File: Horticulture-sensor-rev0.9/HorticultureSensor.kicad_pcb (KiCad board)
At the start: 2 copper layers, 23 parts, among them J1 Conn_01x04, J2 Conn_02x05_Odd_Even, J3 Conn_01x03, J4 Conn_01x04, J5 Conn_01x03, J6 Conn_01x02, J7 Conn_01x02, J8 Conn_01x01_MountingPin, J9 Conn_01x01_MountingPin, Q1 IRLML2030TRPBF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

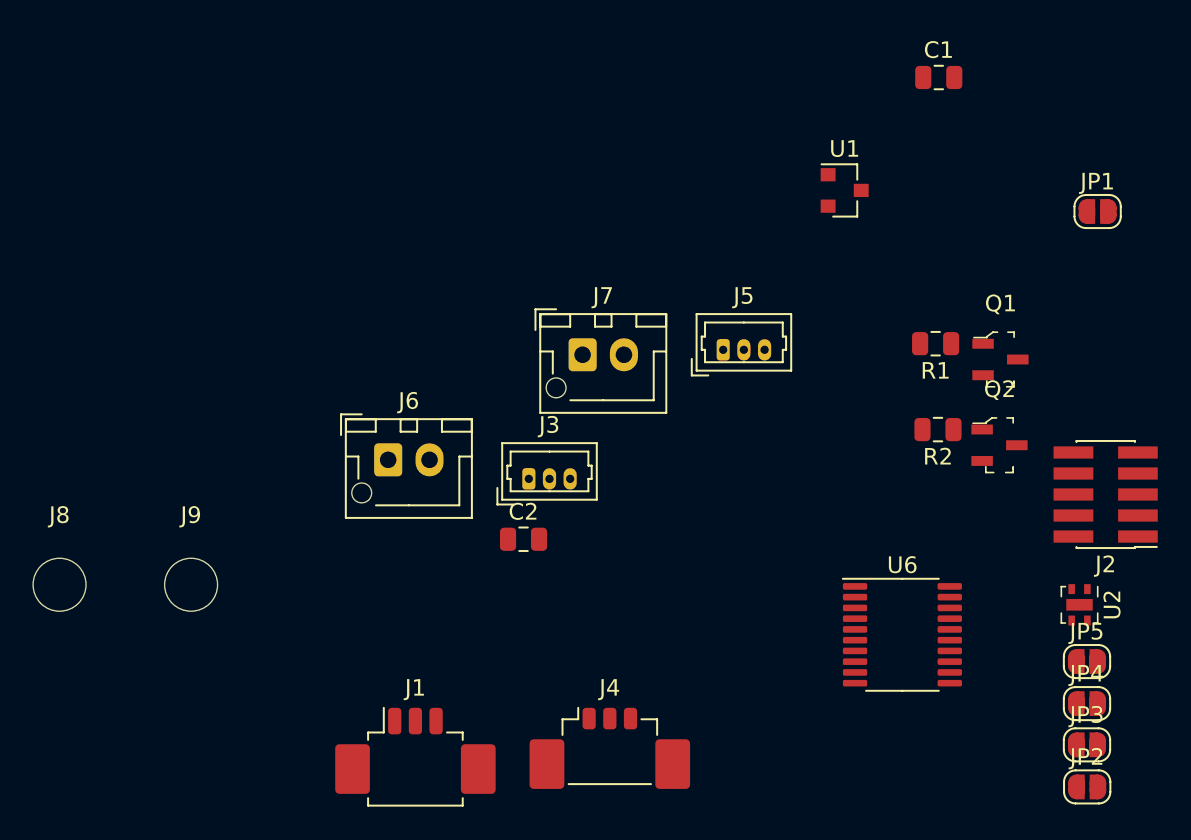
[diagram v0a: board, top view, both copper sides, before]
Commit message: Initial sensor design
Almost finished, need to work out how power connection should work.
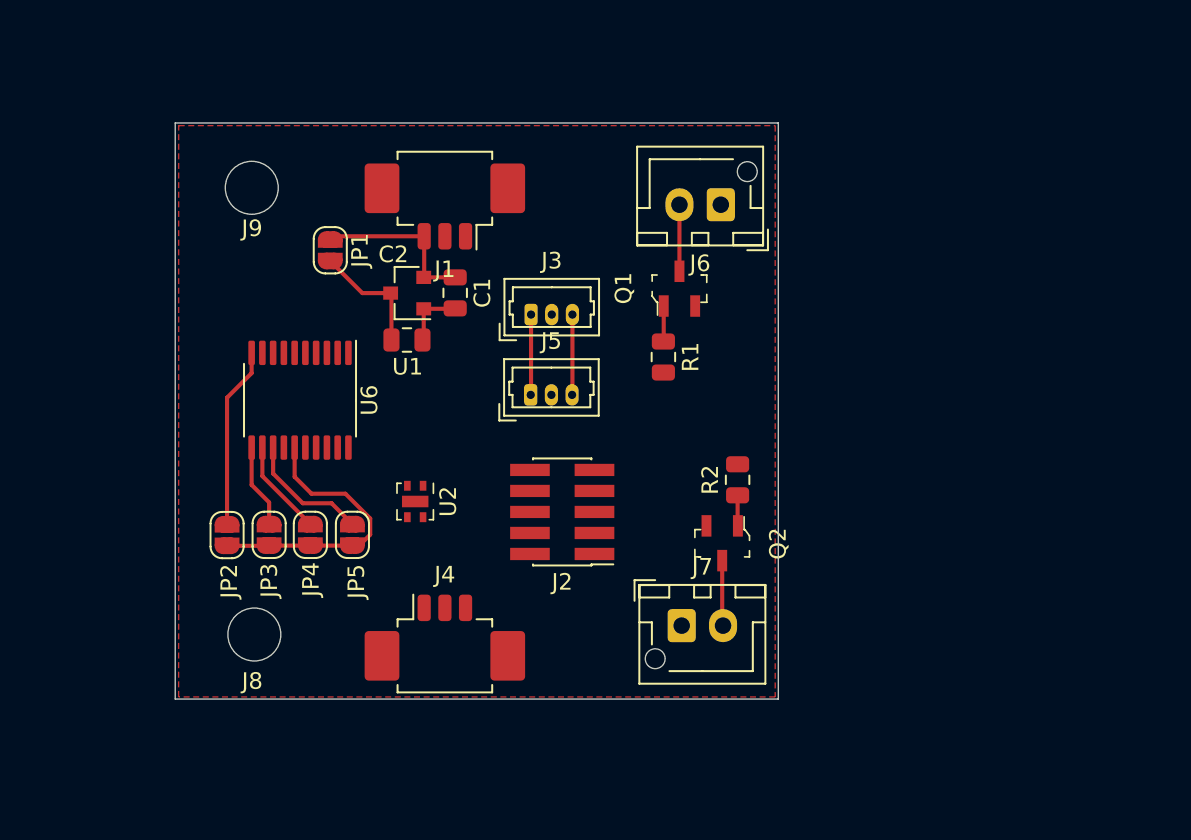
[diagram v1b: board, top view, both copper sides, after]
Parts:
- J4: footprint Connector_Molex:Molex_PicoBlade_53398-0371_1x03-1MP_P1.25mm_Vertical -> Connector_Molex:Molex_PicoBlade_53261-0371_1x03-1MP_P1.25mm_Horizontal
- moved JP2 54.2 mm to (146.7, 136.0), turned to 270 degrees
- moved JP3 51.0 mm to (149.2, 136.0), turned to 270 degrees
- moved JP4 48.0 mm to (151.7, 136.0), turned to 270 degrees
- moved JP1 46.4 mm to (152.9, 118.8), turned to 270 degrees
- moved JP5 45.1 mm to (154.3, 136.0), turned to 270 degrees
- moved U2 40.6 mm to (158.1, 134.0)
- moved U6 39.1 mm to (151.1, 127.8), turned to 270 degrees
- moved J1 34.1 mm to (159.8, 115.5), turned to 180 degrees
- moved J2 32.9 mm to (166.9, 134.6)
- moved C1 32.0 mm to (160.5, 121.4), turned to 270 degrees
- moved U1 27.2 mm to (157.6, 121.4), turned to 180 degrees
- moved J6 25.3 mm to (176.5, 116.0), turned to 180 degrees
- moved J9 24.3 mm to (148.2, 115.0)
- moved Q1 19.9 mm to (174.0, 121.1), turned to 90 degrees
- moved Q2 17.8 mm to (176.6, 136.5), turned to 270 degrees
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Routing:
- net GND: track 0.00 -> 26.0 mm
- net +3V3: track 0.00 -> 12.2 mm
- net i2c-addr_0: track 0.00 -> 11.0 mm
- net VCC: track 0.00 -> 10.2 mm
- net i2c-addr_3: track 0.00 -> 7.63 mm
- net i2c-addr_2: track 0.00 -> 5.83 mm
- net i2c-addr_1: track 0.00 -> 5.06 mm
- net control_0: track 0.00 -> 4.02 mm
- net control_1: track 0.00 -> 3.95 mm
- net Net-(Q1-Pad1): track 0.00 -> 2.15 mm
- net Net-(Q2-Pad1): track 0.00 -> 1.85 mm
- added copper zone on F.Cu, net GND
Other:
- board outline added: 36.5 x 34.8 mm

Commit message: Working on sensor board
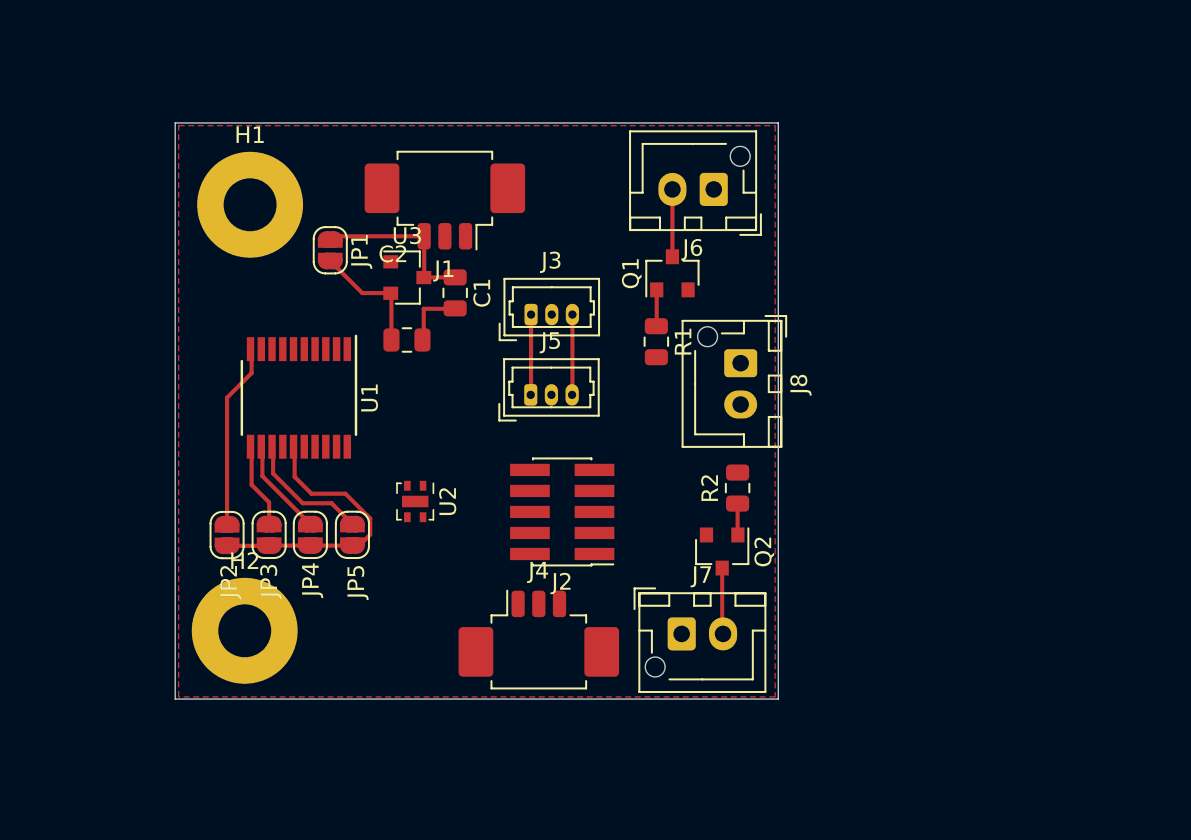
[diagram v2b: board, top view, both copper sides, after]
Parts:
- removed J9: Conn_01x01_MountingPin, MountingHole:MountingHole_3.2mm_M3
- removed U6: STM32F030F4Px, Package_SO:TSSOP-20_4.4x6.5mm_P0.65mm
- added H1: MountingHole_Pad, MountingHole:MountingHole_3.2mm_M3_Pad, F.Cu at (148.1, 116.0)
- added H2: MountingHole_Pad, MountingHole:MountingHole_3.2mm_M3_Pad, F.Cu at (147.8, 141.8)
- added U3: MCP1700-3302E_TO, Package_TO_SOT_SMD:SOT-23, F.Cu at (157.6, 120.4)
- J8: value Conn_01x01_MountingPin -> Conn_01x02; footprint MountingHole:MountingHole_3.2mm_M3 -> Connector_JST:JST_XH_B2B-XH-AM_1x02_P2.50mm_Vertical
- Q1, Q2: footprint digikey-footprints:SOT-23-3 -> Package_TO_SOT_SMD:SOT-23
- U1: value MCP1700-3302E_TO -> STM32F030F4Px; footprint Package_TO_SOT_SMD:SOT-23 -> Package_SO:TSSOP-20_4.4x6.5mm_P0.65mm
- moved J8 33.7 mm to (177.7, 125.6), turned to 270 degrees
- moved U1 9.11 mm to (151.0, 127.7), turned to 270 degrees
- moved J4 5.68 mm to (165.5, 142.6)
- moved J6 1.02 mm to (176.1, 115.1)
- moved Q1 1.02 mm to (173.6, 120.2)
- moved R1 1.02 mm to (172.6, 124.3)
- moved J7 0.50 mm to (174.2, 142.0)
- moved Q2 0.50 mm to (176.6, 137.0)
- moved R2 0.50 mm to (177.5, 133.1)
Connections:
- C1 pad 2: GND -> 12V-
- C2 pad 2: GND -> 12V-
- J1 pad 3: VCC -> +3V3
- J2 pad 3: GND -> 12V-
- J2 pad 5: GND -> 12V-
- J2 pad 6: (no net) -> Net-(J2-Pad6)
- J2 pad 7: (no net) -> Net-(J2-Pad7)
- J2 pad 8: (no net) -> Net-(J2-Pad8)
- J2 pad 9: (no net) -> Net-(J2-Pad9)
- J3 pad 3: GND -> 12V-
- J4 pad 3: VCC -> +3V3
- J5 pad 3: GND -> 12V-
- J6 pad 1: VCC -> 12V+
- J7 pad 1: VCC -> 12V+
- J8 pad 1: GND -> 12V-
- JP2 pad 2: GND -> 12V-
- JP3 pad 2: GND -> 12V-
- JP4 pad 2: GND -> 12V-
- JP5 pad 2: GND -> 12V-
- Q1 pad 2: GND -> 12V-
- Q2 pad 2: GND -> 12V-
- U1 pad 1: GND -> Net-(U1-Pad1)
- U1 pad 2: VCC -> Net-(U1-Pad2)
- U1 pad 3: +3V3 -> Net-(U1-Pad3)
- U2 pad 4: GND -> 12V-
- U2 pad 5: GND -> 12V-
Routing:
- net GND: track 26.0 -> 0.00 mm
- net 12V-: track 0.00 -> 26.0 mm
- added copper zone on F.Cu, net 12V-
- removed copper zone on F.Cu, net GND
